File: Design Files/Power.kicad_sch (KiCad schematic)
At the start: 66 parts, among them J1 1053101208, U13 TLVM13630RDHR, U14 TLVM13630RDHR, U2 AT24CS64-MAHM, U4 LM74700QDBVRQ1, U5 CSD18511Q5A, U6 CSD18511Q5A, U7 LM74700QDBVRQ1, U8 CSD18511Q5A, U9 LM74700QDBVRQ1

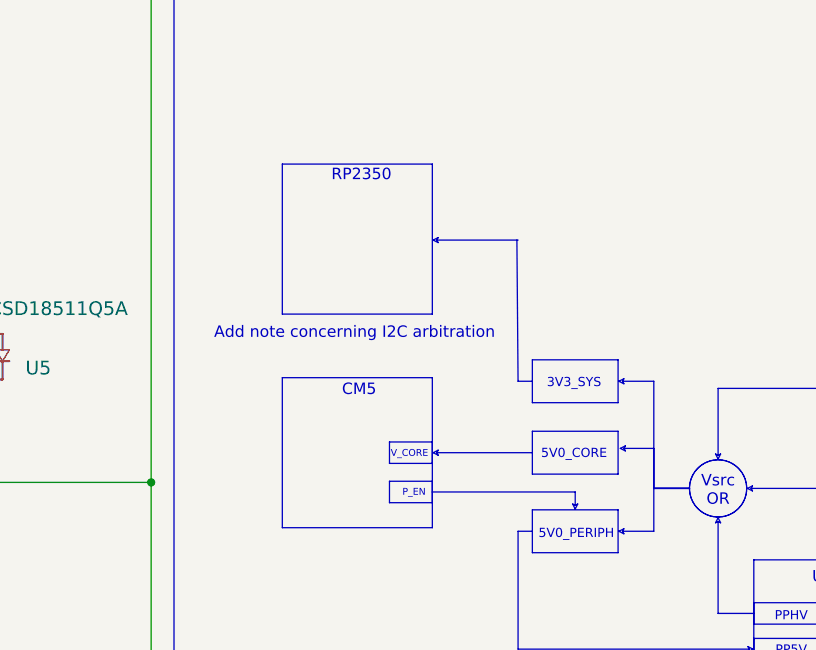
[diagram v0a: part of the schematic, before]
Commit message: More interface interconnects
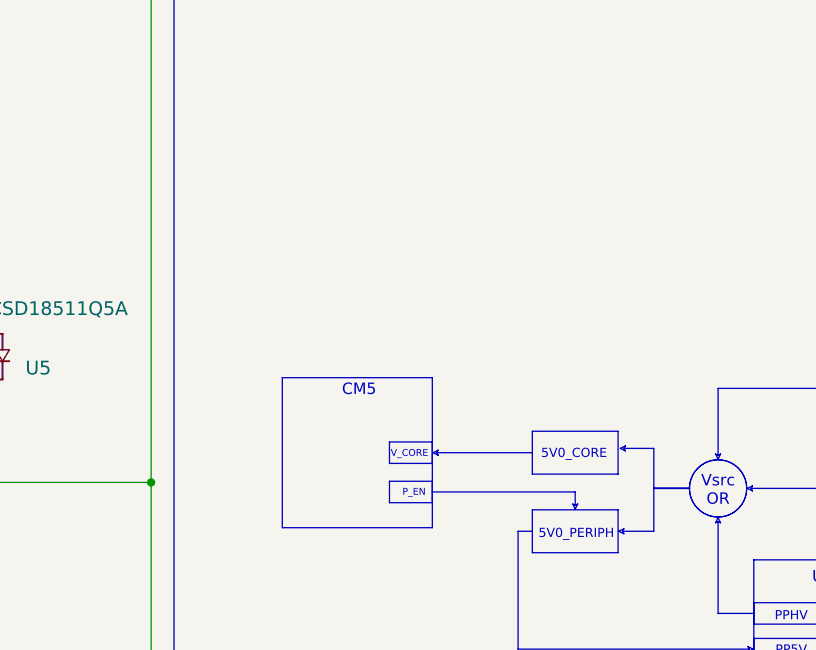
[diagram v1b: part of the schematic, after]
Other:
- note removed: "3V3_SYS"
- note removed: "Add note concerning I2C arbitration"
- note removed: "RP2350"
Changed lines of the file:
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@@
 	(polyline
 		(pts
-			(xy 313.1843 194.6592) (xy 296.5156 194.6592) (xy 296.5156 177.9905) (xy 313.1843 177.9905) (xy 313.1843 194.6592)
-		)
-		(stroke
-			(width 0)
-			(type solid)
-		)
-		(fill
-			(type none)
-		)
-	)
-	(polyline
-		(pts
 			(xy 313.1843 218.3924) (xy 296.5156 218.3924) (xy 296.5156 201.7236) (xy 313.1843 201.7236) (xy 313.1843 218.3924)
 		)
@@
 	(polyline
 		(pts
-			(xy 313.69 186.436) (xy 313.8289 186.7138) (xy 313.2732 186.436) (xy 313.8289 186.1581) (xy 313.69 186.436)
-		)
-		(stroke
-			(width 0)
-			(type solid)
-		)
-		(fill
-			(type color)
-			(color 0 0 0 0)
-		)
-	)
-	(polyline
-		(pts
 			(xy 333.8218 212.4392) (xy 324.2968 212.4392) (xy 324.2968 207.6767) (xy 333.8218 207.6767) (xy 333.8218 212.4392)
 		)
@@
 	(polyline
 		(pts
-			(xy 333.8218 204.5017) (xy 324.2968 204.5017) (xy 324.2968 199.7392) (xy 333.8218 199.7392) (xy 333.8218 204.5017)
-		)
-		(stroke
-			(width 0)
-			(type solid)
-		)
-		(fill
-			(type color)
-			(color 255 255 255 1)
-		)
-	)
-	(polyline
-		(pts
 			(xy 393.3531 216.408) (xy 383.8281 216.408) (xy 383.8281 211.6455) (xy 393.3531 211.6455) (xy 393.3531 216.408)
 		)
@@
 		)
 	)
-	(polyline
-		(pts
-			(xy 334.3275 202.1205) (xy 334.4664 202.3983) (xy 333.9107 202.1205) (xy 334.4664 201.8427) (xy 334.3275 202.1205)
-		)
-		(stroke
-			(width 0)
-			(type solid)
-		)
-		(fill
-			(type color)
-			(color 0 0 0 0)
-		)
-	)
 	(bezier
 		(pts
@@
 		)
 	)
-	(text "3V3_SYS"
-		(exclude_from_sim no)
-		(at 328.93 202.438 0)
-		(effects
-			(font
-				(size 1.016 1.016)
-			)
-		)
-	)
 	(text "Psense\nI2C"
 		(exclude_from_sim no)
@@
 		)
 	)
-	(text "Add note concerning I2C arbitration"
-		(exclude_from_sim no)
-		(at 304.546 196.85 0)
-		(effects
-			(font
-				(size 1.27 1.27)
-			)
-		)
-	)
 	(text "PP5V"
 		(exclude_from_sim no)
@@
 		)
 	)
-	(text "RP2350"
-		(exclude_from_sim no)
-		(at 305.308 179.324 0)
-		(effects
-			(font
-				(size 1.27 1.27)
-			)
-		)
-	)
 	(text "CM5"
 		(exclude_from_sim no)
@@
 		)
 	)
-	(polyline
-		(pts
-			(xy 322.7093 186.436) (xy 313.69 186.436)
-		)
-		(stroke
-			(width 0)
-			(type solid)
-		)
-	)
 	(wire
 		(pts
@@
 		)
 	)
-	(polyline
-		(pts
-			(xy 337.7906 214.0267) (xy 337.7906 202.1205)
-		)
-		(stroke
-			(width 0)
-			(type solid)
-		)
-	)
 	(wire
 		(pts
@@
 		)
 	)
-	(polyline
-		(pts
-			(xy 337.7906 202.1205) (xy 334.3275 202.1205)
-		)
-		(stroke
-			(width 0)
-			(type solid)
-		)
-	)
 	(wire
 		(pts
@@
 		)
 	)
-	(polyline
-		(pts
-			(xy 324.2968 202.1205) (xy 322.7093 202.1205)
-		)
-		(stroke
-			(width 0)
-			(type solid)
-		)
-	)
 	(wire
 		(pts
@@
 		)
 	)
-	(polyline
-		(pts
-			(xy 322.7093 202.1205) (xy 322.58 186.436)
-		)
-		(stroke
-			(width 0)
-			(type solid)
-		)
-	)

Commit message: Additional layout updates
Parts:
- R10, R13: value R_US -> 53.6k
- R11, R14, R8: value R_US -> 10k
- R7, R9: value R_US -> 25.5k
- U3: value ~ -> (none)
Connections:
- net GND: now also U13.26 (PG); no longer C19.1, C21.1, C26.1, C28.1, C30.1, C31.1, C33.1, R14.1, U13.18 (VIN), U13.19 (VIN), U13.3 (VIN), U13.4 (VIN), U14.18 (VIN), U14.19 (VIN), U14.3 (VIN), U14.4 (VIN), U4.4 (CATHODE), U5.5 (D), U5.6 (D), U5.7 (D), U5.8 (D), U5.9 (D), U6.5 (D), U6.6 (D), U6.7 (D), U6.8 (D), U6.9 (D), U7.4 (CATHODE), U8.5 (D), U8.6 (D), U8.7 (D), U8.8 (D), U8.9 (D), U9.4 (CATHODE)
- net 5V0_C_RAW: now reaches C11.1, C20.1, FB1.1, R13.1, U13.10 (VOUT), U13.12 (VOUT), U13.13 (VOUT), U13.14 (VOUT), U13.15 (VOUT), U13.22 (VLDOIN), U13.30 (VOUT), U13.7 (VOUT), U13.8 (VOUT), U13.9 (VOUT)
- net LDO_1V5: now reaches C27.1, U3.4 (LDO_1V5)
- net 5V0_P_RAW: now reaches C14.1, C22.1, C4.1, FB2.1, R10.1, U14.10 (VOUT), U14.12 (VOUT), U14.13 (VOUT), U14.14 (VOUT), U14.15 (VOUT), U14.22 (VLDOIN), U14.30 (VOUT), U14.7 (VOUT), U14.8 (VOUT), U14.9 (VOUT)
- net VIN_3V3: now reaches C8.1, U3.38 (VIN_3V3)
- net USB_DRAIN: now reaches U3.15 (DRAIN), U3.30 (DRAIN), U3.40 (DRAIN_PAD)
- new net V_COMMON: C19.1, C21.1, C26.1, C28.1, C30.1, C31.1, C33.1, R14.1, U13.18 (VIN), U13.19 (VIN), U13.3 (VIN), U13.4 (VIN), U14.18 (VIN), U14.19 (VIN), U14.3 (VIN), U14.4 (VIN), U4.4 (CATHODE), U5.5 (D), U5.6 (D), U5.7 (D), U5.8 (D), U5.9 (D), U6.5 (D), U6.6 (D), U6.7 (D), U6.8 (D), U6.9 (D), U7.4 (CATHODE), U8.5 (D), U8.6 (D), U8.7 (D), U8.8 (D), U8.9 (D), U9.4 (CATHODE)
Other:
- note added: "~400kHz"
- note removed: "Swap FETs to CSD18563Q5A"
- moved on the sheet: C1, C12, C15, C17, C18, C2, C42, C43, C44, C45, C46, C47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

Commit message: Misc
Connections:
- net G_BATT: now reaches U5.4 (G), U7.5 (GATE)
- net VCAP_AUX: now reaches C13.2, U4.1 (VCAP)
- net VCAP_BATT: now reaches C9.2, U7.1 (VCAP)
- net G_AUX: now reaches U4.5 (GATE), U6.4 (G)
- net G_USB: now reaches U8.4 (G), U9.5 (GATE)
- net VCAP_USB: now reaches C23.2, U9.1 (VCAP)
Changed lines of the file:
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@@
 	)
 	(junction
-		(at 255.27 154.94)
-		(diameter 0)
-		(color 0 0 0 0)
-	)
-	(junction
 		(at 199.39 134.62)
 		(diameter 0)
@@
 	(wire
 		(pts
-			(xy 255.27 154.94) (xy 255.27 153.67)
-		)
-		(stroke
-			(width 0)
-			(type default)
-		)
-	)
-	(wire
-		(pts
 			(xy 50.8 106.68) (xy 60.96 106.68)
 		)
@@
 		)
 	)
+	(label "G_USB"
+		(at 247.65 254 90)
+		(effects
+			(font
+				(size 1.27 1.27)
+			)
+			(justify left bottom)
+		)
+	)
+	(label "VCAP_AUX"
+		(at 199.39 163.83 270)
+		(effects
+			(font
+				(size 1.27 1.27)
+			)
+			(justify right bottom)
+		)
+	)
 	(label "V_USB"
 		(at 161.29 242.57 0)
@@
 		)
 	)
+	(label "G_AUX"
+		(at 247.65 147.32 90)
+		(effects
+			(font
+				(size 1.27 1.27)
+			)
+			(justify left bottom)
+		)
+	)
 	(label "VIN_3V3"
 		(at 92.71 182.88 0)
@@
 		)
 	)
+	(label "VCAP_USB"
+		(at 199.39 270.51 270)
+		(effects
+			(font
+				(size 1.27 1.27)
+			)
+			(justify right bottom)
+		)
+	)
 	(label "I2Cc_SCL"
 		(at 78.74 270.51 0)
@@
 		)
 	)
+	(label "G_BATT"
+		(at 247.65 203.2 90)
+		(effects
+			(font
+				(size 1.27 1.27)
+			)
+			(justify left bottom)
+		)
+	)
 	(label "V_AUX"
 		(at 199.39 134.62 0)
@@
 		)
 	)
+	(label "VCAP_BATT"
+		(at 199.39 220.98 270)
+		(effects
+			(font
+				(size 1.27 1.27)
+			)
+			(justify right bottom)
+		)
+	)
